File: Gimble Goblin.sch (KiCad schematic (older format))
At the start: 14 parts

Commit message: github is hard
I lack the knowledge to properly manipulate files, this should be better now. it was previously a mess
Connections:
- net labels added: SI, SO
- wire segments 97 -> 91
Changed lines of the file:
@@
 Text GLabel 1700 5350 0    50   Input ~ 0
 SS
+Text GLabel 1700 5150 0    50   Input ~ 0
+SI
+Text GLabel 1700 5250 0    50   Input ~ 0
+SO
 Text GLabel 1700 5450 0    50   Input ~ 0
 SCK
@@
 Wire Wire Line
 	3200 4850 3200 5550
-Wire Wire Line
-	1900 2200 1250 2200
-Wire Wire Line
-	1250 2200 1250 5250
-Wire Wire Line
-	1250 5250 1700 5250
-Wire Wire Line
-	1700 5150 1350 5150
-Wire Wire Line
-	1350 5150 1350 2300
-Wire Wire Line
-	1350 2300 1900 2300
 $EndSCHEMATC

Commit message: 0.0.3 First Complete Design - Ready for Review
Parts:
- removed J?: RJ45_LED, symbol Connector:RJ45_LED
- removed J? (x3): CONN_03JST-PTH-VERT, JST-3-PTH-VERT, symbol SparkFun-Connectors:CONN_03JST-PTH-VERT
- added J1: RJ45_LED_Shielded, RJHSE-5381:AMPHENOL_RJHSE-5381, symbol Connector:RJ45_LED_Shielded
- added J2, J3, J4: CONN_03, Connectors:1X03, symbol SparkFun-Connectors:CONN_03
- U1: renamed from U?; footprint (none) -> Package_TO_SOT_THT:TO-220-3_Horizontal_TabDown
- gave numbers to parts that had none: 9
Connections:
- net labels removed: SCK, SI, SO, SS
- wire segments 91 -> 104
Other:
- moved on the sheet: A1, C1, C2, U1, U2, U3, Y1

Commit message: Re-organized schematic
Fixed schematic,
Updated PCB and compomnents
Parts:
- removed J1: RJ45_LED_Shielded, RJHSE-5381:AMPHENOL_RJHSE-5381, symbol Connector:RJ45_LED_Shielded
- removed J2, J3, J4: CONN_03, Connectors:1X03, symbol SparkFun-Connectors:CONN_03
- removed R1: 1M, Resistor_SMD:R_0603_1608Metric, symbol Device:R
- removed R2, R3: 10k, Resistor_SMD:R_0603_1608Metric, symbol Device:R
- added C3, C6: 0.1uF, Capacitor_SMD:C_0603_1608Metric, symbol Device:C
- added C4: 220uF, Capacitor_THT:CP_Radial_D7.5mm_P2.50mm, symbol Device:CP
- added C5, C7: 100uF, Capacitor_THT:CP_Radial_D5.0mm_P2.50mm, symbol Device:CP
- added J1: Conn_02x03_Odd_Even, Connector_PinHeader_2.54mm:PinHeader_2x03_P2.54mm_Vertical, symbol Connector_Generic:Conn_02x03_Odd_Even
- added J2, J3, J4: Conn_01x03_Male, Connector_PinHeader_2.54mm:PinHeader_1x03_P2.54mm_Vertical, symbol Connector:Conn_01x03_Male
- added R1: 1M, Resistor_SMD:R_0603_1608Metric, symbol Device:R_US
- added R2, R3: 10k, Resistor_SMD:R_0603_1608Metric, symbol Device:R_US
- added U4: L7805, Package_TO_SOT_SMD:SOT-223, symbol Regulator_Linear:L7805
- U1: footprint Package_TO_SOT_THT:TO-220-3_Horizontal_TabDown -> Package_TO_SOT_SMD:SOT-223
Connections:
- net labels added: +12V, +5V, +5VA, CAM, C_RX, C_TX, Gx, Gy, MISO, MOSI, SCK, nCS
- wire segments 104 -> 89
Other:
- note added: "CAN Controller"
- note added: "CAN Transciever"
- note added: "Camera"
- note added: "Main Board & Power\nInterface"
- note added: "Microcontroller - 328P"
- note added: "Primary Power 5V - 1A"
- note added: "Servo Connections"
- note added: "Servo Power"
- note removed: "CAN Communication using MCP2515 and ATA6560"
- moved on the sheet: A1, C1, C2, U2, U3, Y1

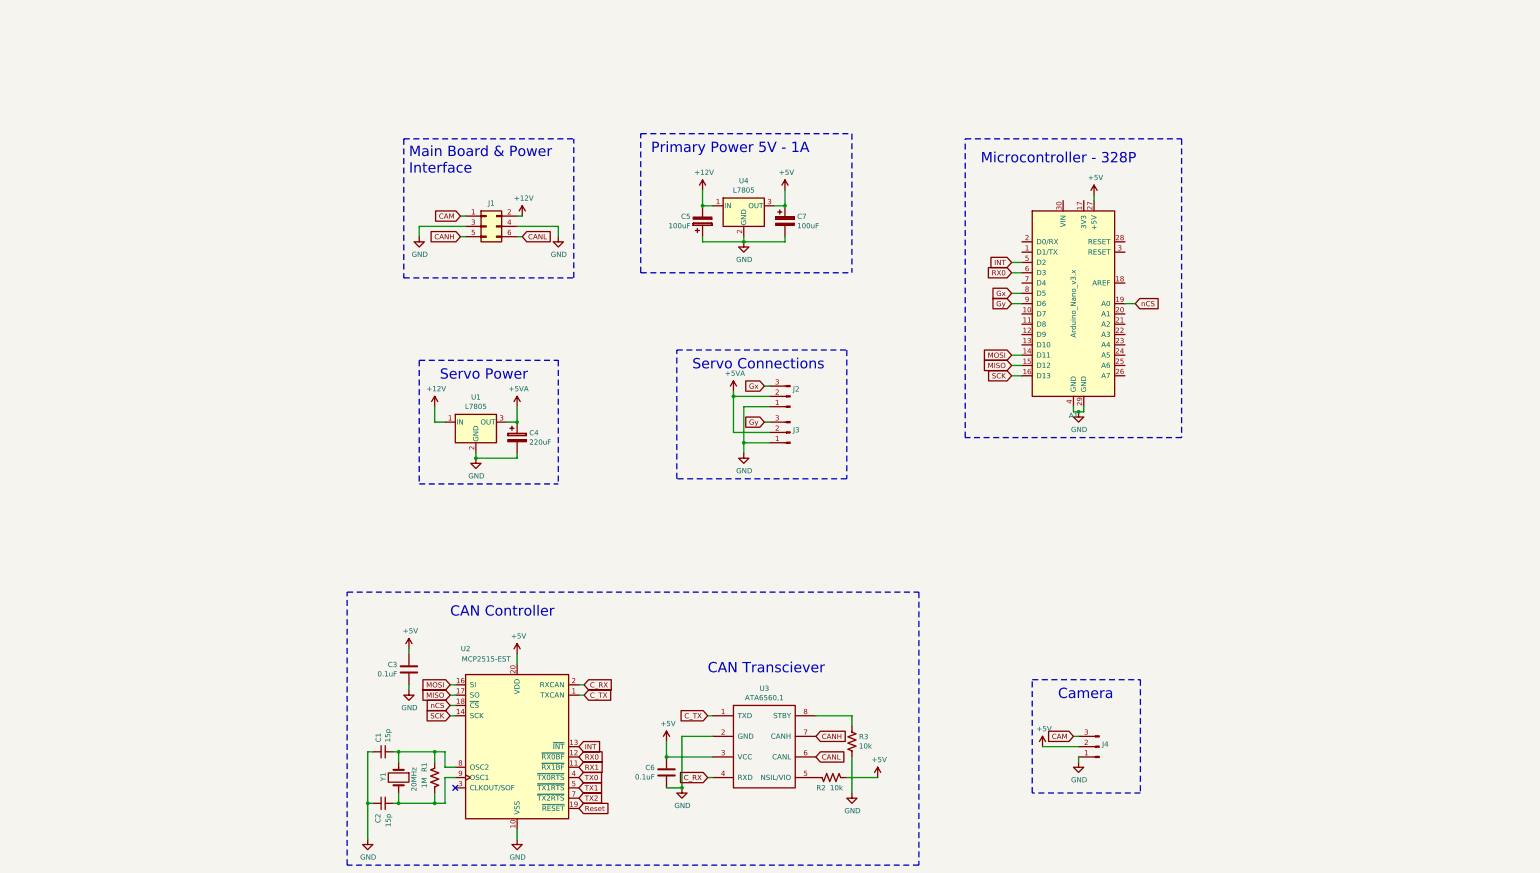
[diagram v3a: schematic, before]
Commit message: Routed PCB
Worked on silkscreen
Finished all routing and via stiching
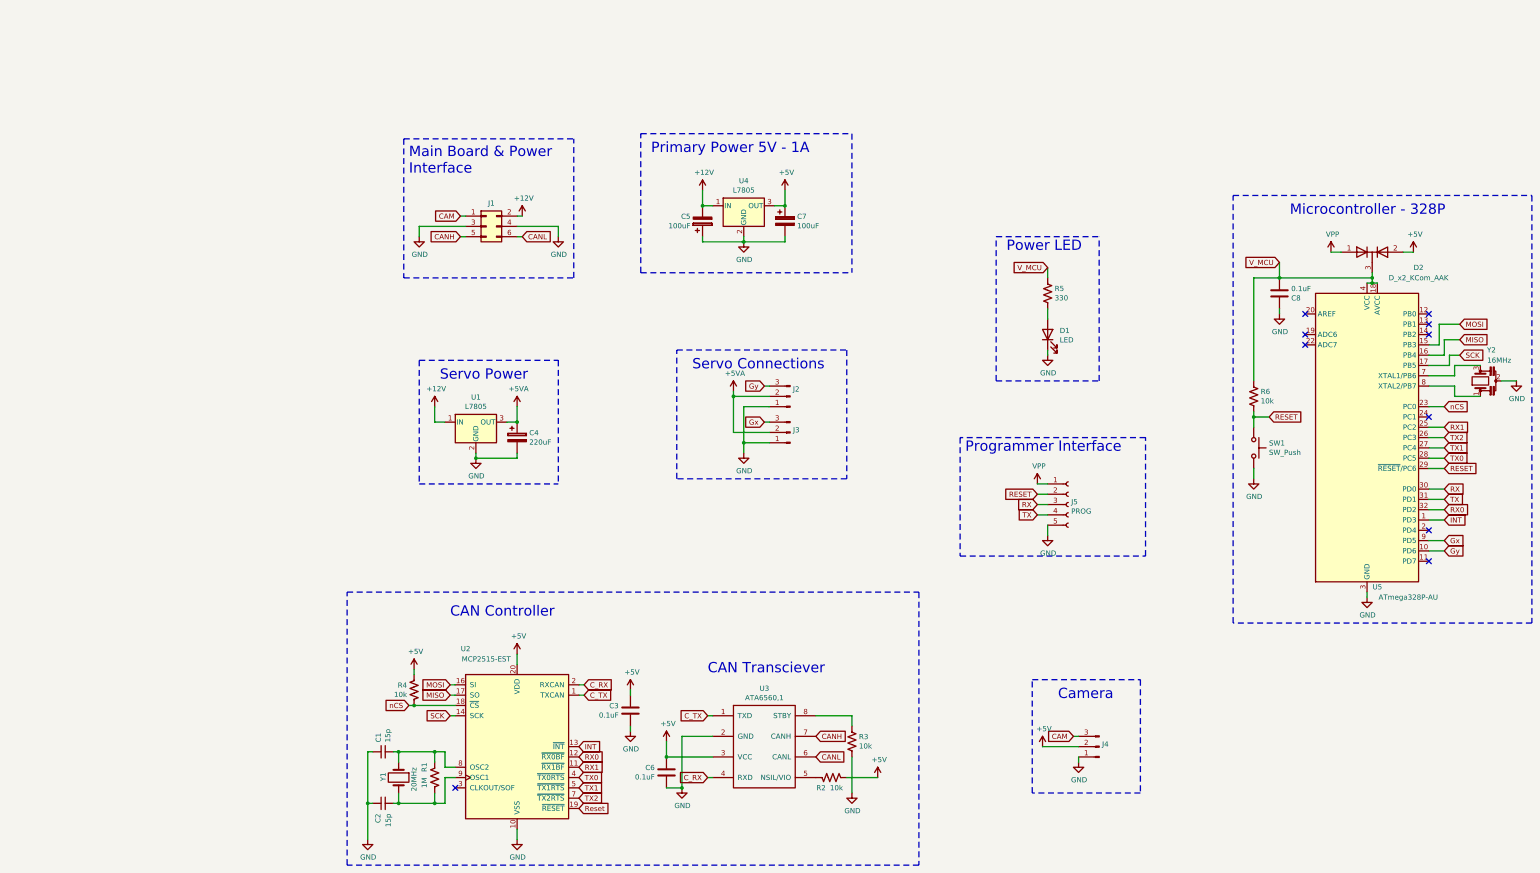
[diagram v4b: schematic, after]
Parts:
- removed A1: Arduino_Nano_v3.x, Module:Arduino_Nano, symbol MCU_Module:Arduino_Nano_v3.x
- added C8: 0.1uF, Capacitor_SMD:C_0603_1608Metric, symbol Device:C
- added D1: LED, LED_SMD:LED_0603_1608Metric, symbol Device:LED
- added D2: D_x2_KCom_AAK, Package_TO_SOT_SMD:SOT-23, symbol Device:D_x2_KCom_AAK
- added J5: PROG, Connector_PinHeader_2.54mm:PinHeader_1x05_P2.54mm_Vertical, symbol Connector:Conn_01x05_Female
- added R4, R6: 10k, Resistor_SMD:R_0603_1608Metric, symbol Device:R_US
- added R5: 330, Resistor_SMD:R_0603_1608Metric, symbol Device:R_US
- added SW1: SW_Push, Button_Switch_THT:SW_PUSH_6mm, symbol Switch:SW_Push
- added U5: ATmega328P-AU, Package_QFP:TQFP-32_7x7mm_P0.8mm, symbol MCU_Microchip_ATmega:ATmega328P-AU
- added Y2: 16MHz, CSTCE16M0V53-R0:OSC_CSTCE16M0V53-R0, symbol Device:Resonator
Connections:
- net +5V: now also D2.2 (A), R4.1
- net GND: now also C8.2, D1.1 (K), J5.5 (Pin_5), SW1.2, U5.21 (GND), U5.3 (GND), U5.5 (GND), Y2.2
- net Gx: now also J3.3 (Pin_3), U5.9 (PD5); no longer J2.3 (Pin_3)
- net Gy: now also J2.3 (Pin_3), U5.10 (PD6); no longer J3.3 (Pin_3)
- net INT: now also U5.1 (PD3)
- net MISO: now also U5.16 (PB4)
- net MOSI: now also U5.15 (PB3)
- net RX0: now also U5.32 (PD2)
- net RX1: now also U5.25 (PC2)
- net SCK: now also U5.17 (PB5)
- net TX0: now also U5.28 (PC5)
- net TX1: now also U5.27 (PC4)
- net TX2: now also U5.26 (PC3)
- net nCS: now also R4.2, U5.23 (PC0)
- new net: U5.7 (XTAL1/PB6), Y2.3
- new net: U5.8 (XTAL2/PB7), Y2.1
- new net: D1.2 (A), R5.2
- new net RESET: J5.2 (Pin_2), R6.2, SW1.1, U5.29 (~RESET~/PC6)
- new net RX: J5.3 (Pin_3), U5.30 (PD0)
- new net TX: J5.4 (Pin_4), U5.31 (PD1)
- new net VPP: D2.1 (A), J5.1 (Pin_1)
- new net V_MCU: C8.1, D2.3 (K), R5.1, R6.1, U5.18 (AVCC), U5.4 (VCC), U5.6 (VCC)
- no-connect marks 1 -> 10
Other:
- note added: "Power LED"
- note added: "Programmer Interface"
- moved on the sheet: C3

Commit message: Implemented review fixes
Generated step file,
Generated gerber zip with drills,
Also verified gerbers online
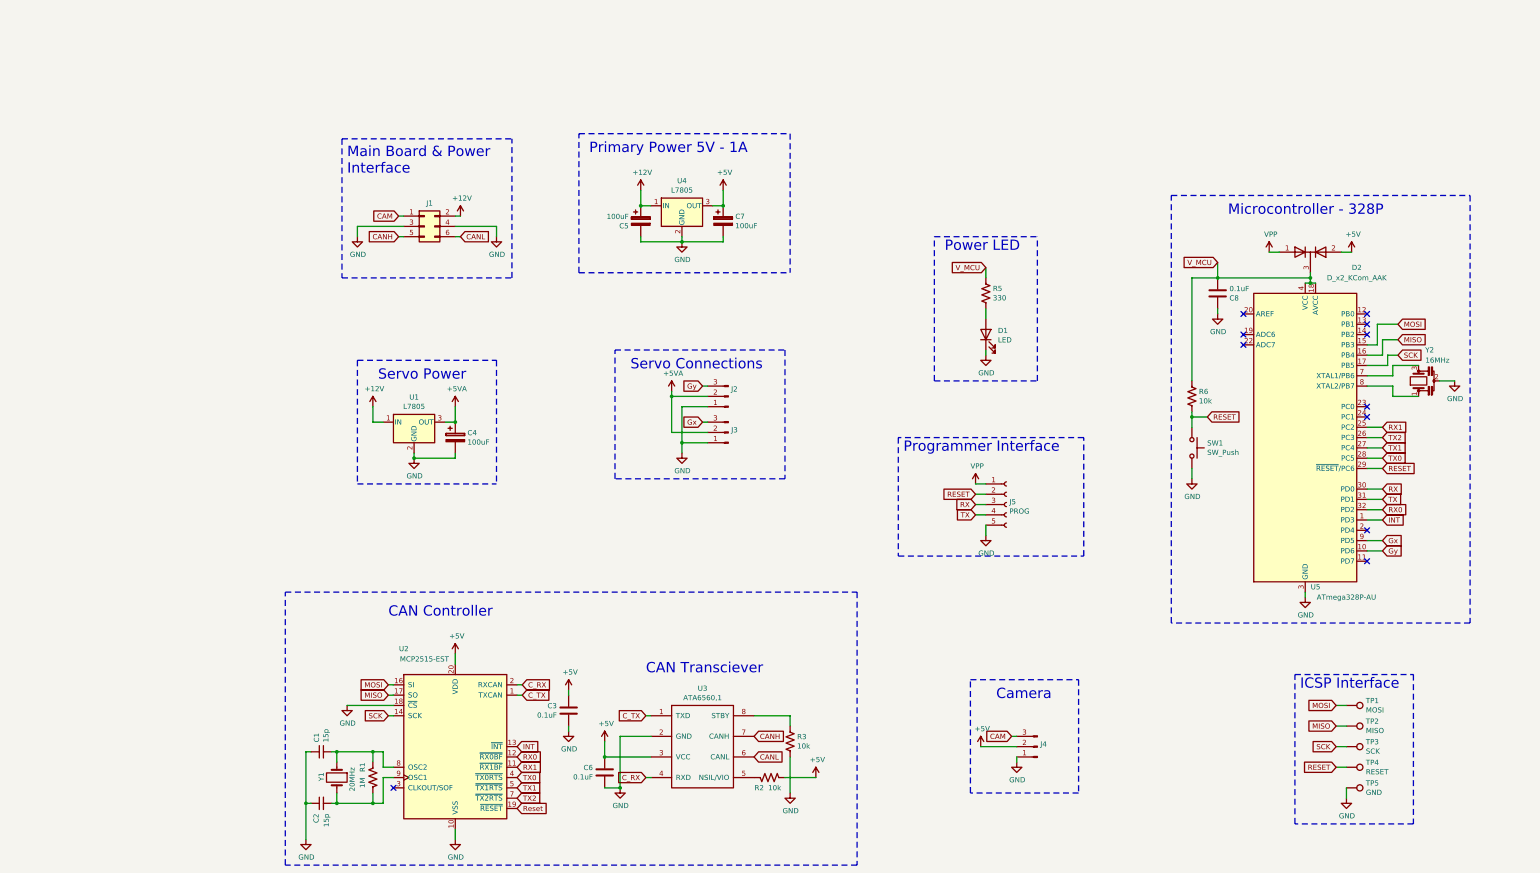
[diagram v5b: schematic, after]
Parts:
- removed R4: 10k, Resistor_SMD:R_0603_1608Metric, symbol Device:R_US
- added TP1: MOSI, TestPoint:TestPoint_Pad_D1.0mm, symbol Connector:TestPoint
- added TP2: MISO, TestPoint:TestPoint_Pad_D1.0mm, symbol Connector:TestPoint
- added TP3: SCK, TestPoint:TestPoint_Pad_D1.0mm, symbol Connector:TestPoint
- added TP4: RESET, TestPoint:TestPoint_Pad_D1.0mm, symbol Connector:TestPoint
- added TP5: GND, TestPoint:TestPoint_Pad_D1.0mm, symbol Connector:TestPoint
- C4: value 220uF -> 100uF; footprint Capacitor_THT:CP_Radial_D7.5mm_P2.50mm -> Capacitor_THT:CP_Radial_D5.0mm_P2.50mm
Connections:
- net +12V: now also C5.1; no longer C5.2
- net GND: now also C5.2, U2.18 (~CS), TP5.1; no longer C5.1
- net MISO: now also TP2.1
- net MOSI: now also TP1.1
- net RESET: now also TP4.1
- net SCK: now also TP3.1
- net nCS: no longer names the net of U5.23 (PC0)
- net nCS: no longer U2.18 (~CS)
- no-connect marks 10 -> 11
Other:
- note added: "ICSP Interface"
- moved on the sheet: C1, C2, C3, C4, C5, C6, C7, C8, D1, D2, J1, J2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
